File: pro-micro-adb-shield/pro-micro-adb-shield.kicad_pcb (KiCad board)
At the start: 2 copper layers, 18 x 43.5 mm, 10 parts, among them J1 Mini-DIN-4, SW1 SW_Push_Dual_Other_PinLayout, SW2 SW_DIP_x04, U1 Arduino_Pro_Micro

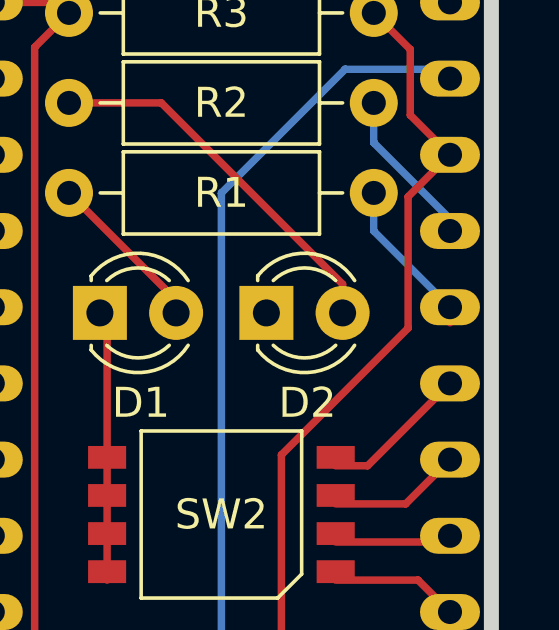
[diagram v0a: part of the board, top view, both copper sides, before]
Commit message: DRC check
remove one sneaky stub trace
refill zones
ignore screaming about silkscreen
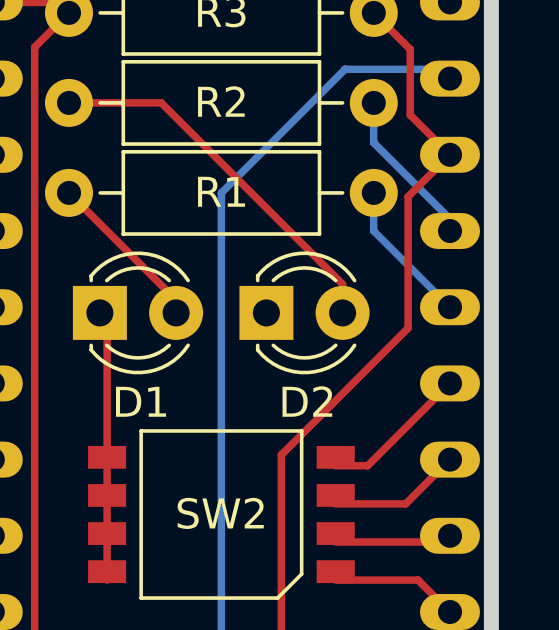
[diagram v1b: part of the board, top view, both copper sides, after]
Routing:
- net LED1: track 5.38 -> 4.86 mm
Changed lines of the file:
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@@
   (segment (start 101.775489 97.625489) (end 104.6 100.45) (width 0.25) (layer "F.Cu") (net 7))
   (segment (start 102.92 77) (end 101.775489 78.144511) (width 0.25) (layer "F.Cu") (net 7))
-  (segment (start 115.62 87.32863) (end 115.62 86.81) (width 0.25) (layer "F.Cu") (net 8))
   (segment (start 113.08 84.27) (end 115.62 86.81) (width 0.25) (layer "B.Cu") (net 8))
   (segment (start 113.08 83) (end 113.08 84.27) (width 0.25) (layer "B.Cu") (net 8))
